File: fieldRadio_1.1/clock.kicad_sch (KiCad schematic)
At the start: 8 parts, among them J12 Conn_01x06, U8 Si5351A-B-GT, Y2 25MHz

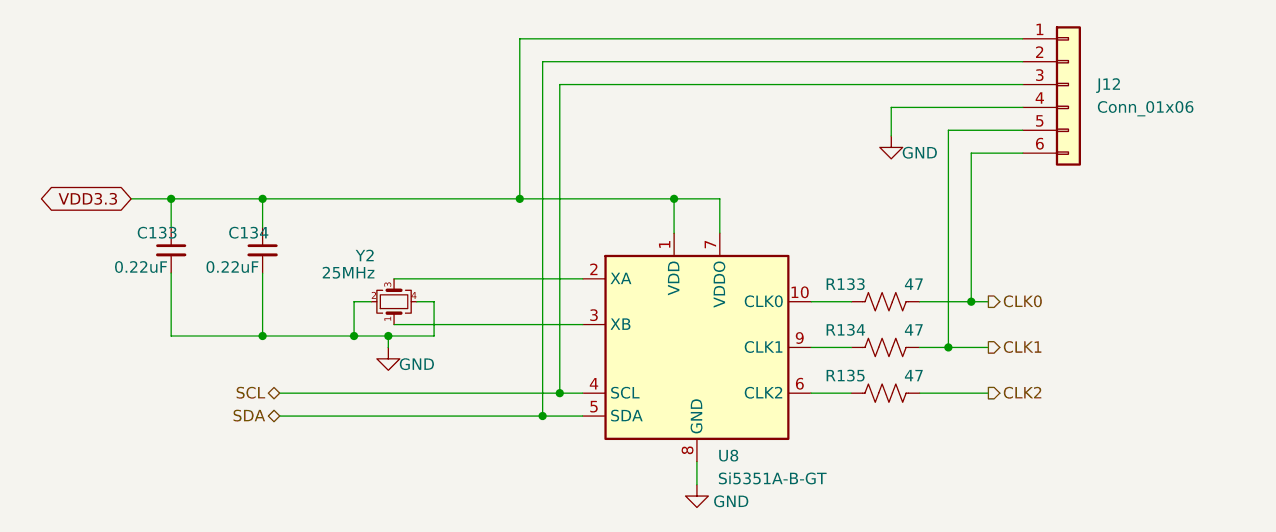
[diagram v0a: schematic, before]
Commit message: Added PTT and TP for clocks
More layout cleanup and tuning.
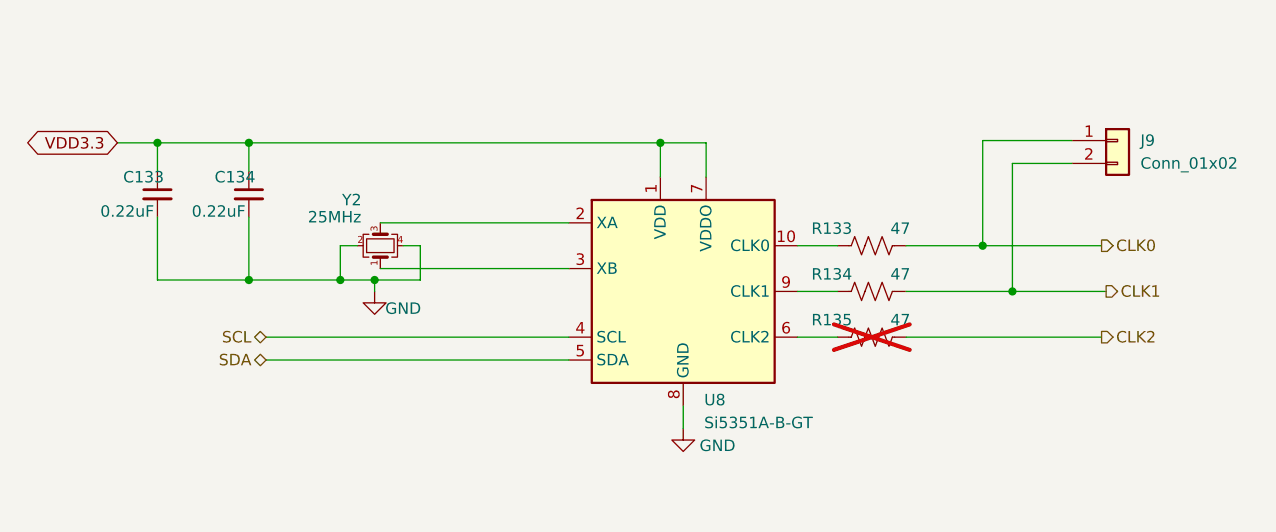
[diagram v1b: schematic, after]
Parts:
- removed J12: Conn_01x06, Connector_PinHeader_2.54mm:PinHeader_1x06_P2.54mm_Vertical, symbol Connector_Generic:Conn_01x06
- added J9: Conn_01x02, Connector_PinHeader_2.54mm:PinHeader_1x02_P2.54mm_Vertical, symbol Connector_Generic:Conn_01x02
- R135: now not fitted
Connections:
- net CLK0: now also J9.1 (Pin_1)
- net CLK1: now also J9.2 (Pin_2)
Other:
- moved on the sheet: C133, C134, R133, R134, U8, Y2
